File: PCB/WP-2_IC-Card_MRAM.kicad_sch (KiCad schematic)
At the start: 30 parts, among them J1 SMS-138-01-G-S, SW1 CUS-14TB, U1 MRxA08xxYSxxx, U2 MIC5317-3.3YD5, U3 4245, U4 4245, U5 4245, U6 4245

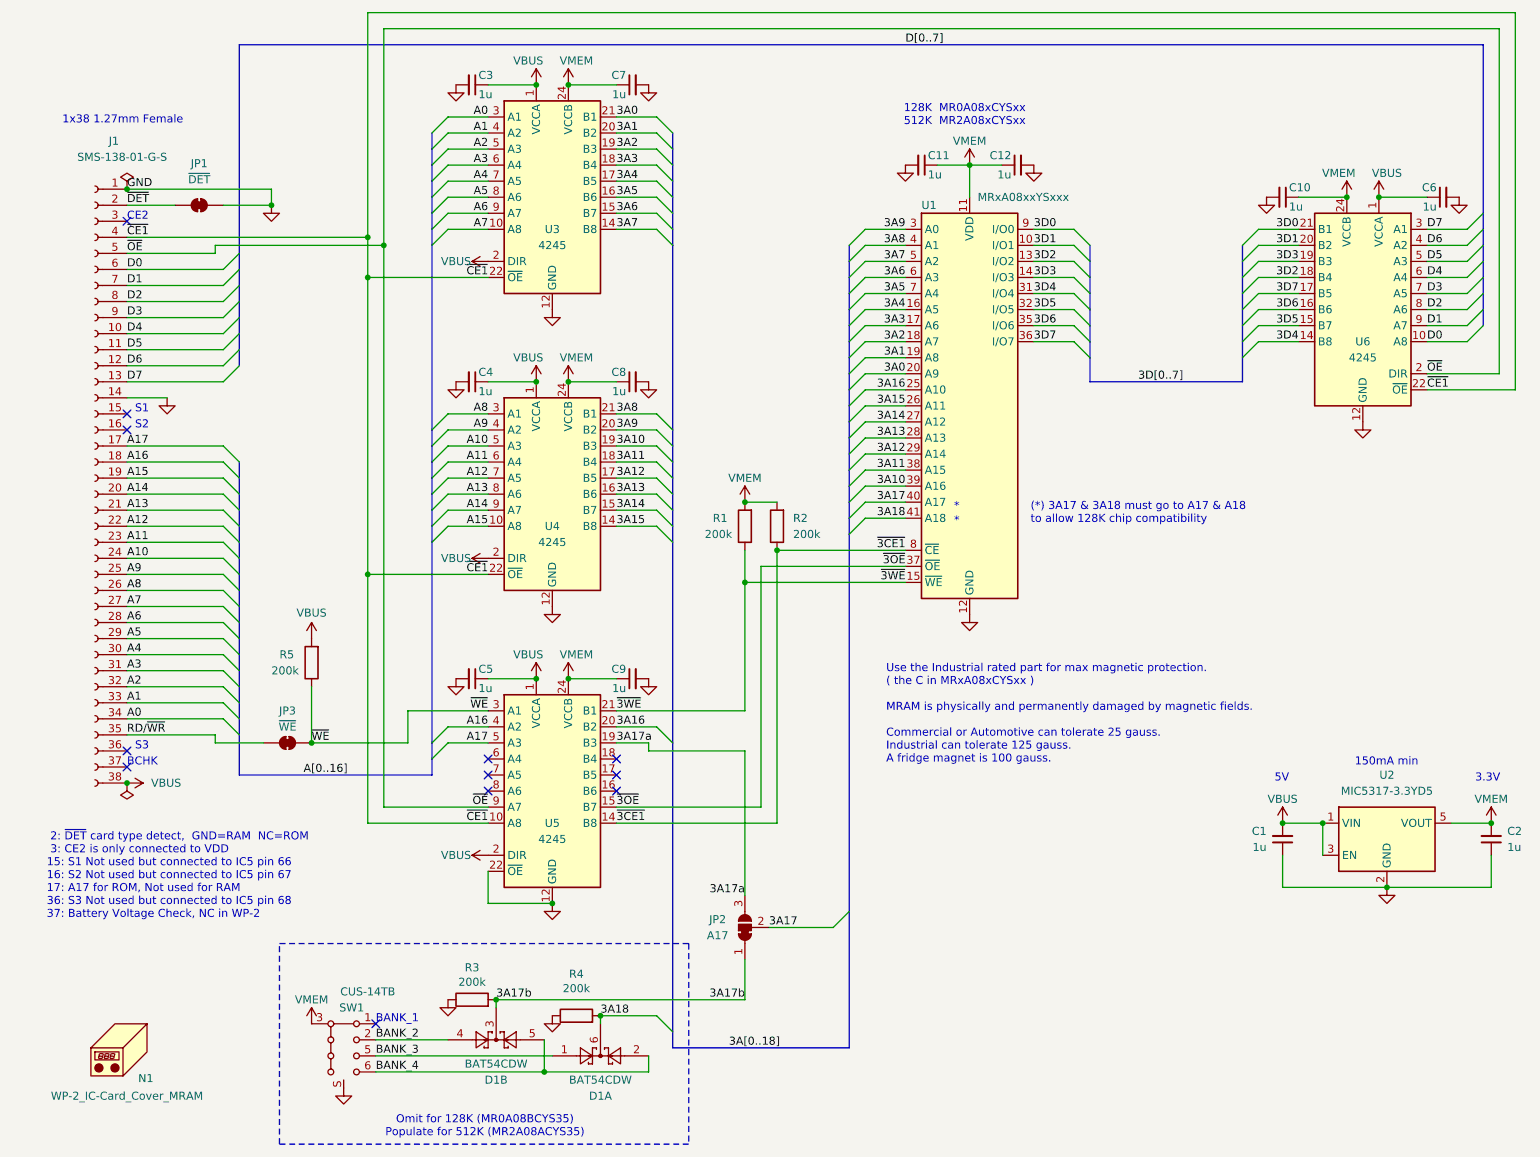
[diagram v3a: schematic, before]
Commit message: mram T2 pin
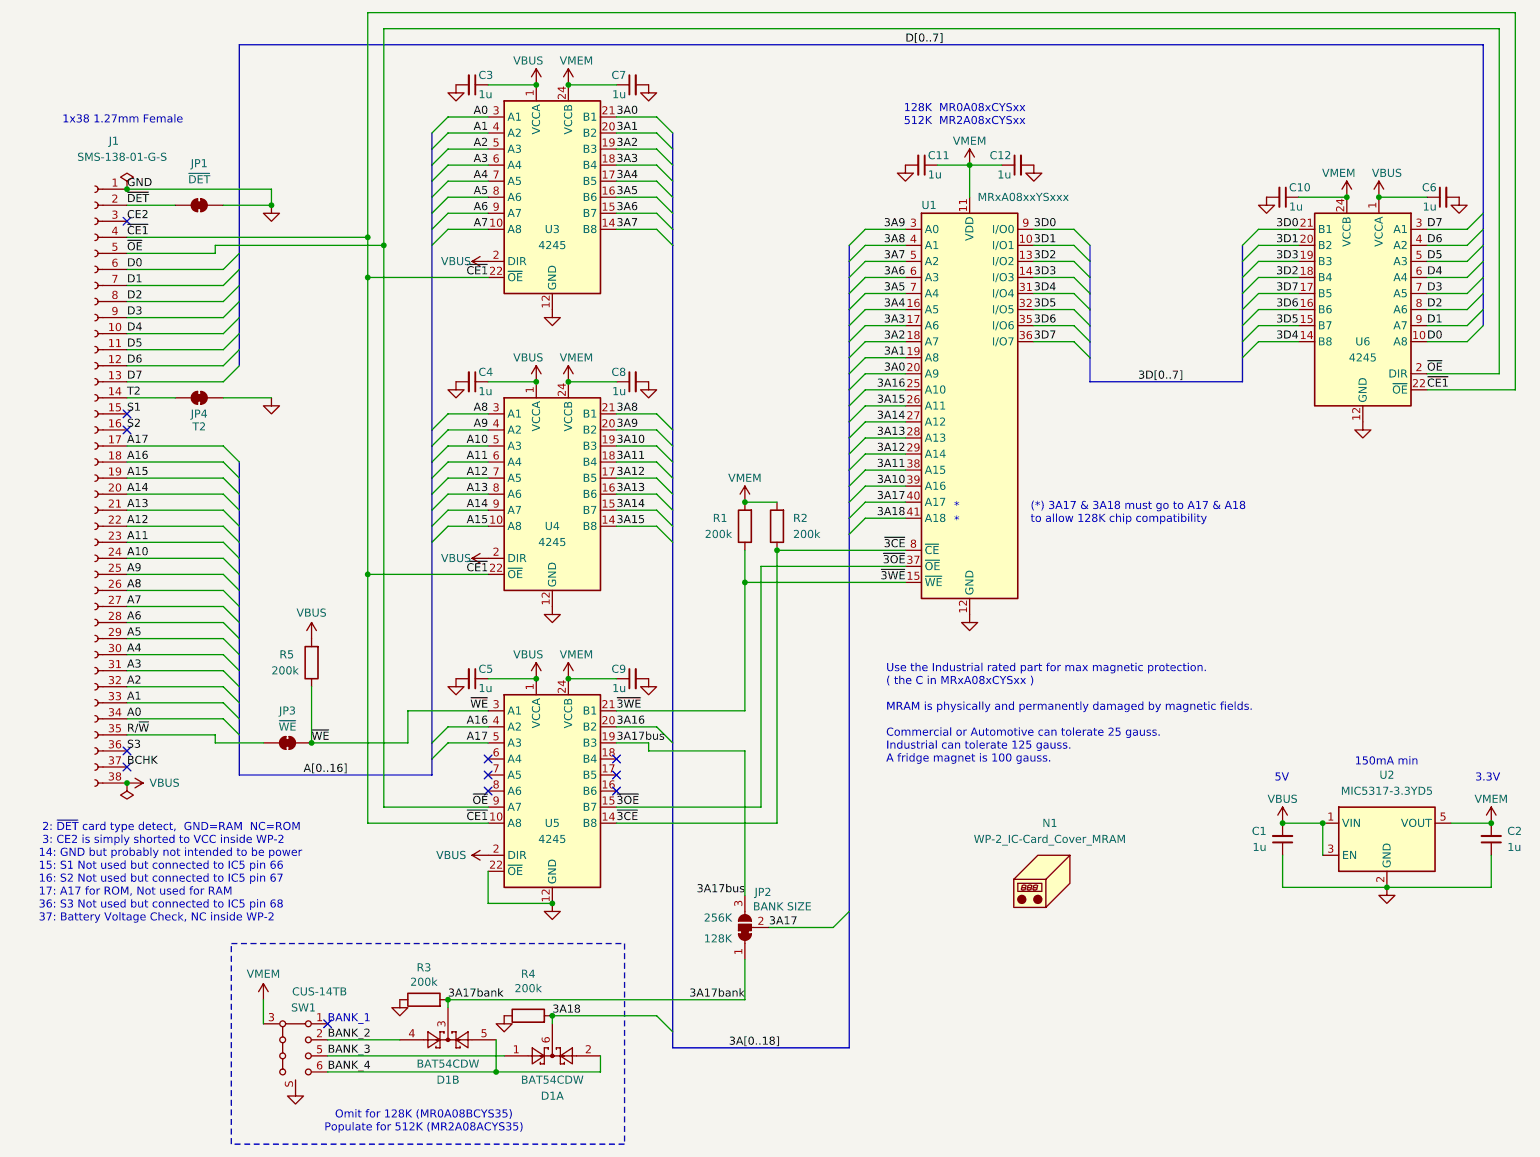
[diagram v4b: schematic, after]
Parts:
- added JP4: T2, 000_LOCAL:SolderJumper-2_P1.3mm_Bridged_RoundedPad1.0x1.5mm, symbol 000_LOCAL:SolderJumper_2_Bridged
- JP2: value A17 -> BANK SIZE; L12 (none) -> 128K; L23 (none) -> 256K
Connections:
- net GND: now also JP4.2 (B); no longer J1.14 (Pin_14)
- net S1: now reaches J1.15 (Pin_15)
- net S2: now reaches J1.16 (Pin_16)
- net CE2: now reaches J1.3 (Pin_3)
- net S3: now reaches J1.36 (Pin_36)
- net BCHK: now reaches J1.37 (Pin_37)
- net 3A17a renamed 3A17bus
- net 3A17b renamed 3A17bank
- net RD/~{WR} renamed R/~{W}
- net ~{3CE1} renamed ~{3CE}
- new net T2: J1.14 (Pin_14), JP4.1 (A)
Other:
- note added: "2: ~{DET} card type detect, GND=RAM NC=ROM 3: CE2 is simply shorted to VCC inside WP-2 14: GND but probably not intended to be power 15: S1 Not used but connected to IC5 pin 66 16: S2 Not used but connected to IC5 pin 67 17: A17 for ROM, Not used for RAM 36: S3 Not used but connected to IC5 pin 68 37: Battery Voltage Check, NC inside WP-2"
- note removed: "2: ~{DET} card type detect, GND=RAM NC=ROM 3: CE2 is only connected to VDD 15: S1 Not used but connected to IC5 pin 66 16: S2 Not used but connected to IC5 pin 67 17: A17 for ROM, Not used for RAM 36: S3 Not used but connected to IC5 pin 68 37: Battery Voltage Check, NC in WP-2"
- note removed: "BCHK"
- note removed: "CE2"
- note removed: "S1"
- note removed: "S2"
- note removed: "S3"
- moved on the sheet: D1A, D1B, N1, R3, R4, SW1

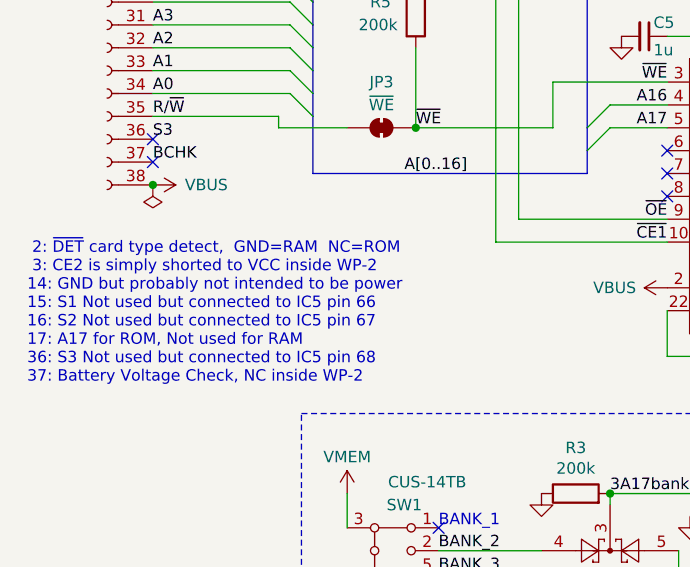
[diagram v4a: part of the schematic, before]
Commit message: SRAM compatible with 512K, pullup /WE, TSOP32 footprint, cfg jumpers
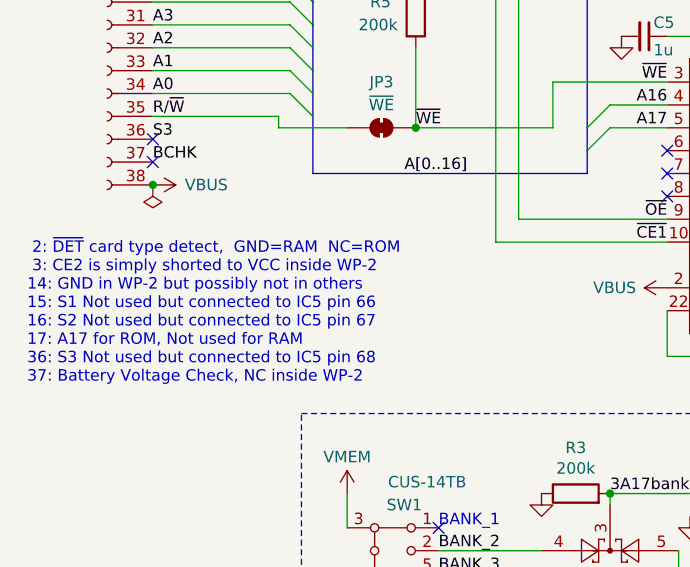
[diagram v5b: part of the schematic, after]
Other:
- note added: "2: ~{DET} card type detect, GND=RAM NC=ROM 3: CE2 is simply shorted to VCC inside WP-2 14: GND in WP-2 but possibly not in others 15: S1 Not used but connected to IC5 pin 66 16: S2 Not used but connected to IC5 pin 67 17: A17 for ROM, Not used for RAM 36: S3 Not used but connected to IC5 pin 68 37: Battery Voltage Check, NC inside WP-2"
- note removed: "2: ~{DET} card type detect, GND=RAM NC=ROM 3: CE2 is simply shorted to VCC inside WP-2 14: GND but probably not intended to be power 15: S1 Not used but connected to IC5 pin 66 16: S2 Not used but connected to IC5 pin 67 17: A17 for ROM, Not used for RAM 36: S3 Not used but connected to IC5 pin 68 37: Battery Voltage Check, NC inside WP-2"
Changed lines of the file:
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@@
 		)
 	)
-	(text " 2: ~{DET} card type detect,  GND=RAM  NC=ROM\n 3: CE2 is simply shorted to VCC inside WP-2\n14: GND but probably not intended to be power\n15: S1 Not used but connected to IC5 pin 66\n16: S2 Not used but connected to IC5 pin 67\n17: A17 for ROM, Not used for RAM\n36: S3 Not used but connected to IC5 pin 68\n37: Battery Voltage Check, NC inside WP-2\n"
+	(text " 2: ~{DET} card type detect,  GND=RAM  NC=ROM\n 3: CE2 is simply shorted to VCC inside WP-2\n14: GND in WP-2 but possibly not in others\n15: S1 Not used but connected to IC5 pin 66\n16: S2 Not used but connected to IC5 pin 67\n17: A17 for ROM, Not used for RAM\n36: S3 Not used but connected to IC5 pin 68\n37: Battery Voltage Check, NC inside WP-2\n"
 		(exclude_from_sim no)
 		(at 17.78 148.59 0)

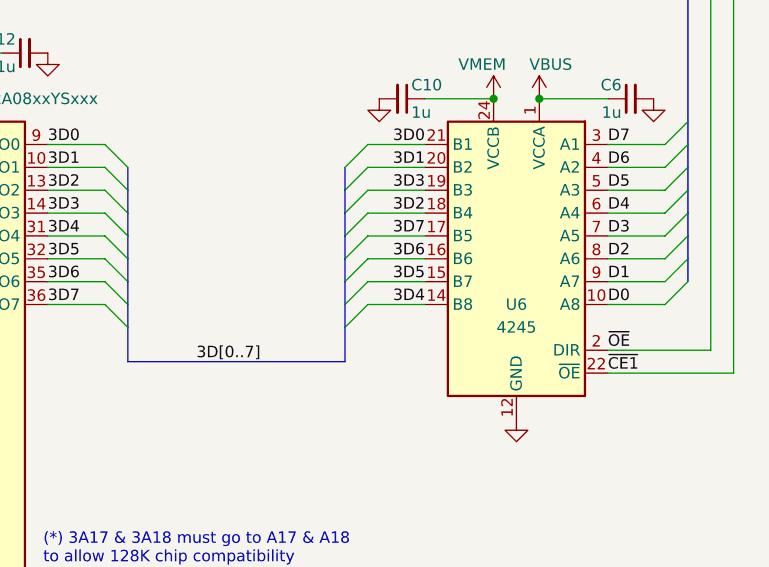
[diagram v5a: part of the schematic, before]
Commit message: refactor cover scad more, cover models makefile, adjust new sram switch & batt positions
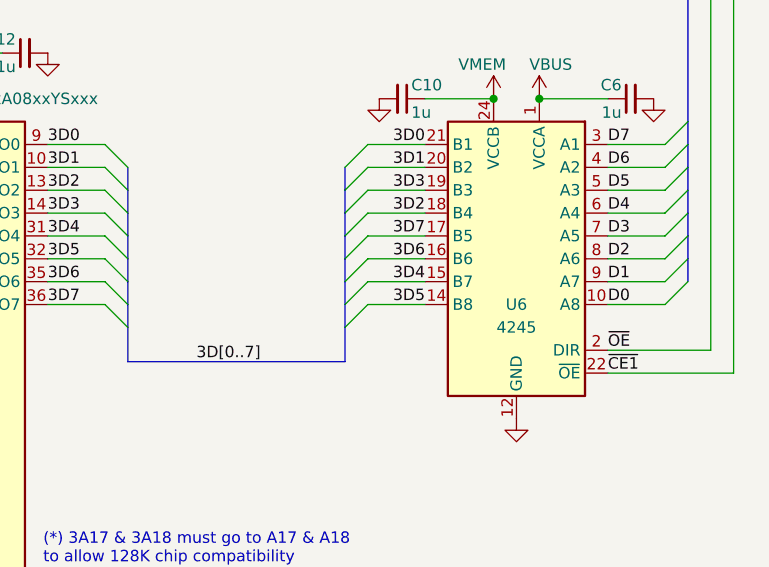
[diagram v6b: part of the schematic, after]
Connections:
- net 3D4: now also U6.15 (B7); no longer U6.14 (B8)
- net 3D5: now also U6.14 (B8); no longer U6.15 (B7)
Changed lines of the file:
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@@
 	)
 	(label "3D4"
-		(at 217.17 72.39 180)
+		(at 217.17 69.85 180)
 		(fields_autoplaced yes)
 		(effects
@@
 	)
 	(label "3D5"
-		(at 217.17 69.85 180)
-		(fields_autoplaced yes)
-		(effects
+		(at 217.17 72.39 180)
+		(fields_autoplaced yes)
+		(effects

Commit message: mram solder jumper footprints & pics
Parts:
- JP1, JP3, JP4: footprint 000_LOCAL:SolderJumper-2_P1.3mm_Bridged_RoundedPad1.0x1.5mm -> 000_LOCAL:SolderJumper-2_Bridged
- JP2: footprint 000_LOCAL:SolderJumper-3_P1.3mm_Bridged12_RoundedPad1.0x1.5mm -> 000_LOCAL:SolderJumper-3_Bridged12
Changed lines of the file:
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@@
 			)
 		)
-		(property "Footprint" "000_LOCAL:SolderJumper-3_P1.3mm_Bridged12_RoundedPad1.0x1.5mm"
+		(property "Footprint" "000_LOCAL:SolderJumper-3_Bridged12"
 			(at 129.54 165.1 0)
 			(effects
@@
 			)
 		)
-		(property "Footprint" "000_LOCAL:SolderJumper-2_P1.3mm_Bridged_RoundedPad1.0x1.5mm"
+		(property "Footprint" "000_LOCAL:SolderJumper-2_Bridged"
 			(at 43.18 50.8 0)
 			(effects
@@
 			)
 		)
-		(property "Footprint" "000_LOCAL:SolderJumper-2_P1.3mm_Bridged_RoundedPad1.0x1.5mm"
+		(property "Footprint" "000_LOCAL:SolderJumper-2_Bridged"
 			(at 57.15 135.89 0)
 			(effects
@@
 			)
 		)
-		(property "Footprint" "000_LOCAL:SolderJumper-2_P1.3mm_Bridged_RoundedPad1.0x1.5mm"
+		(property "Footprint" "000_LOCAL:SolderJumper-2_Bridged"
 			(at 43.18 81.28 0)
 			(effects
